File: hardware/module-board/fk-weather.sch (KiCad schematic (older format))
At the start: 99 parts, among them J1 MICRO-USB, J2 CONN_01X03, J3 CONN_01X06, J4 Conn_01x02, J5 Conn_01x01, J6 CONN-HDR-2x5, J7 Conn_01x01, J8 Conn_01x01, J9 Conn_01x01, M1 MOUNT_HOLE, M2 MOUNT_HOLE, M3 MOUNT_HOLE, M4 MOUNT_HOLE, Q1 2N7002LT1G, Q2 2N7002LT1G, Q3 2N7002LT1G, Q4 2N7002LT1G, SW1 SPNO, U1 ATSAMD21G18A-AU, U101 TSL2591, U102 MPL3115A2, U103 BNO055, U104 SHT31, U2 MCP1700T-XXX2E, U3 MAX4466, U4 S25FL1xxK0XM, Y1 FC-135, Y101 FC-135

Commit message: Adding PCB/sch for the wind/rain connectors.
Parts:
- removed C105, C107: 22pF, Capacitors_SMD:C_0603_HandSoldering, symbol CAPACITOR-CERAMIC
- removed C106, C108: 100nF, Capacitors_SMD:C_0603_HandSoldering, symbol CAPACITOR-CERAMIC
- removed J5, J8: Conn_01x01, Measurement_Points:Measurement_Point_Round-SMD-Pad_Small, symbol Conn_01x01
- removed R101, R102, R103: 10K, Resistors_SMD:R_0603_HandSoldering, symbol RESISTOR
- removed R26, R27: 4.7K, Resistors_SMD:R_0603_HandSoldering, symbol RESISTOR
- removed U103: BNO055, conservify:BNO055, symbol BNO055-RESCUE-fk-weather
- removed Y101: FC-135, RocketScreamKicadLibrary:ABS07, symbol CRYSTAL
- added D10, D11, D6, D7, D8, D9: DIODE, RocketScreamKicadLibrary:SOD-123, symbol DIODE
- added J10, J11: Conn_01x06, conservify:wurth_615006138421, symbol Conn_01x06
- added R30, R31, R32, R33, R34: 1K, Resistors_SMD:R_0603_HandSoldering, symbol RESISTOR
- R22, R23: value 0R -> 1K; footprint conservify:SJ_SHORTED -> Resistors_SMD:R_0603_HandSoldering; spn1 (none) -> 603-RC0603FR-07330RL
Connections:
- net labels added: FLASH_CS, RAIN, RAIN_2, RAIN_5, WIND_DIR, WIND_SPEED
- net labels removed: D10, D11, D5, D6, SCL2, SDA2
- wire segments 300 -> 297
- no-connect marks 15 -> 11
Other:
- moved on the sheet: C10, C101, C102, C103, C104, C11, C12, C13, C15, C16, C17, C18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

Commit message: Removing sensors from module board.
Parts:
- removed C101: 1uF, Capacitors_SMD:C_0603_HandSoldering, symbol CAPACITOR-CERAMIC
- removed C102, C103, C109: 100nF, Capacitors_SMD:C_0603_HandSoldering, symbol CAPACITOR-CERAMIC
- removed C104: 10uF, Capacitors_SMD:C_0603_HandSoldering, symbol CAPACITOR-CERAMIC
- removed R18, R19, R20, R21, R24, R25: 0R, conservify:SJ_SHORTED, symbol RESISTOR
- removed U101: TSL2591, Housings_DFN_QFN:DFN-6-1EP_2x2mm_Pitch0.65mm, symbol TSL2591
- removed U102: MPL3115A2, conservify:DFN-8-1EP_5x2.55mm_Pitch1.25mm_98ASA002260D, symbol MPL3115A2
- removed U104: SHT31, conservify:SHT3x, symbol SHT31
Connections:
- wire segments 297 -> 255
- no-connect marks 11 -> 7

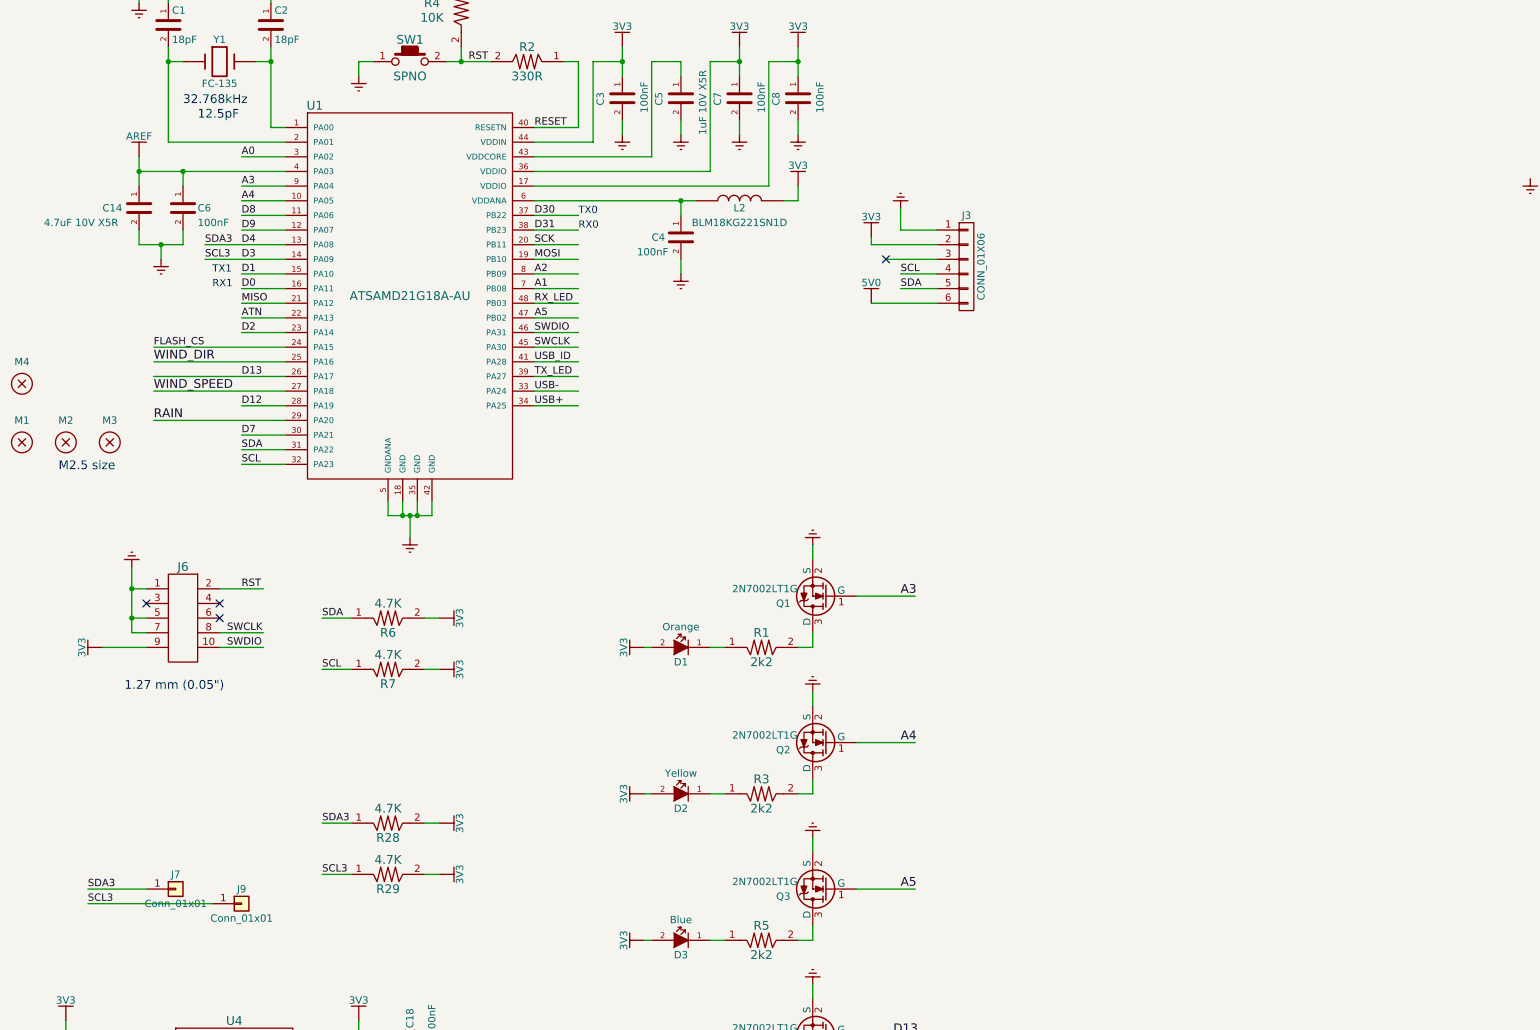
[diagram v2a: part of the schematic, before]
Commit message: Wire up the I2C buses to the header.
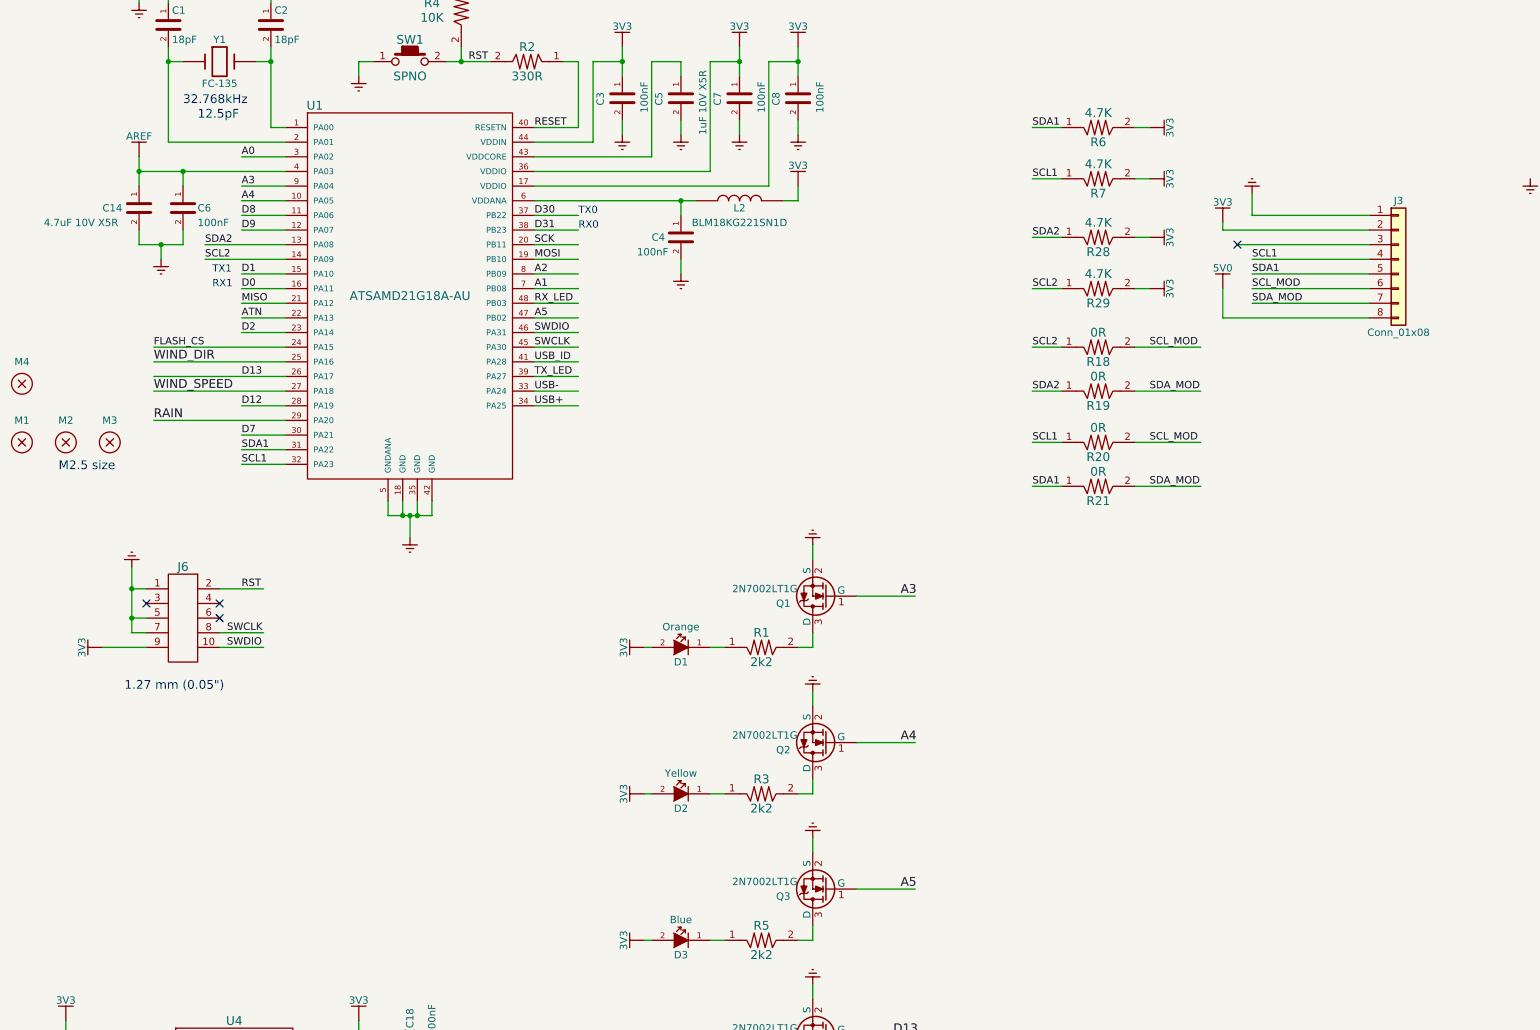
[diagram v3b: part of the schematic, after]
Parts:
- removed J3: CONN_01X06, Socket_Strips:Socket_Strip_Straight_1x06_Pitch2.54mm, symbol CONN_01X06
- removed J7, J9: Conn_01x01, Measurement_Points:Measurement_Point_Round-SMD-Pad_Small, symbol Conn_01x01
- added J3: Conn_01x08, Socket_Strips:Socket_Strip_Straight_1x08_Pitch2.54mm, symbol Conn_01x08
- added R18, R19, R20, R21: 0R, conservify:SJ_SHORTED, symbol RESISTOR
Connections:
- net labels added: SCL1, SCL2, SCL_MOD, SDA1, SDA2, SDA_MOD
- net labels removed: D3, D4, SCL, SCL3, SDA, SDA3
- wire segments 255 -> 264
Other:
- moved on the sheet: R28, R29, R6, R7

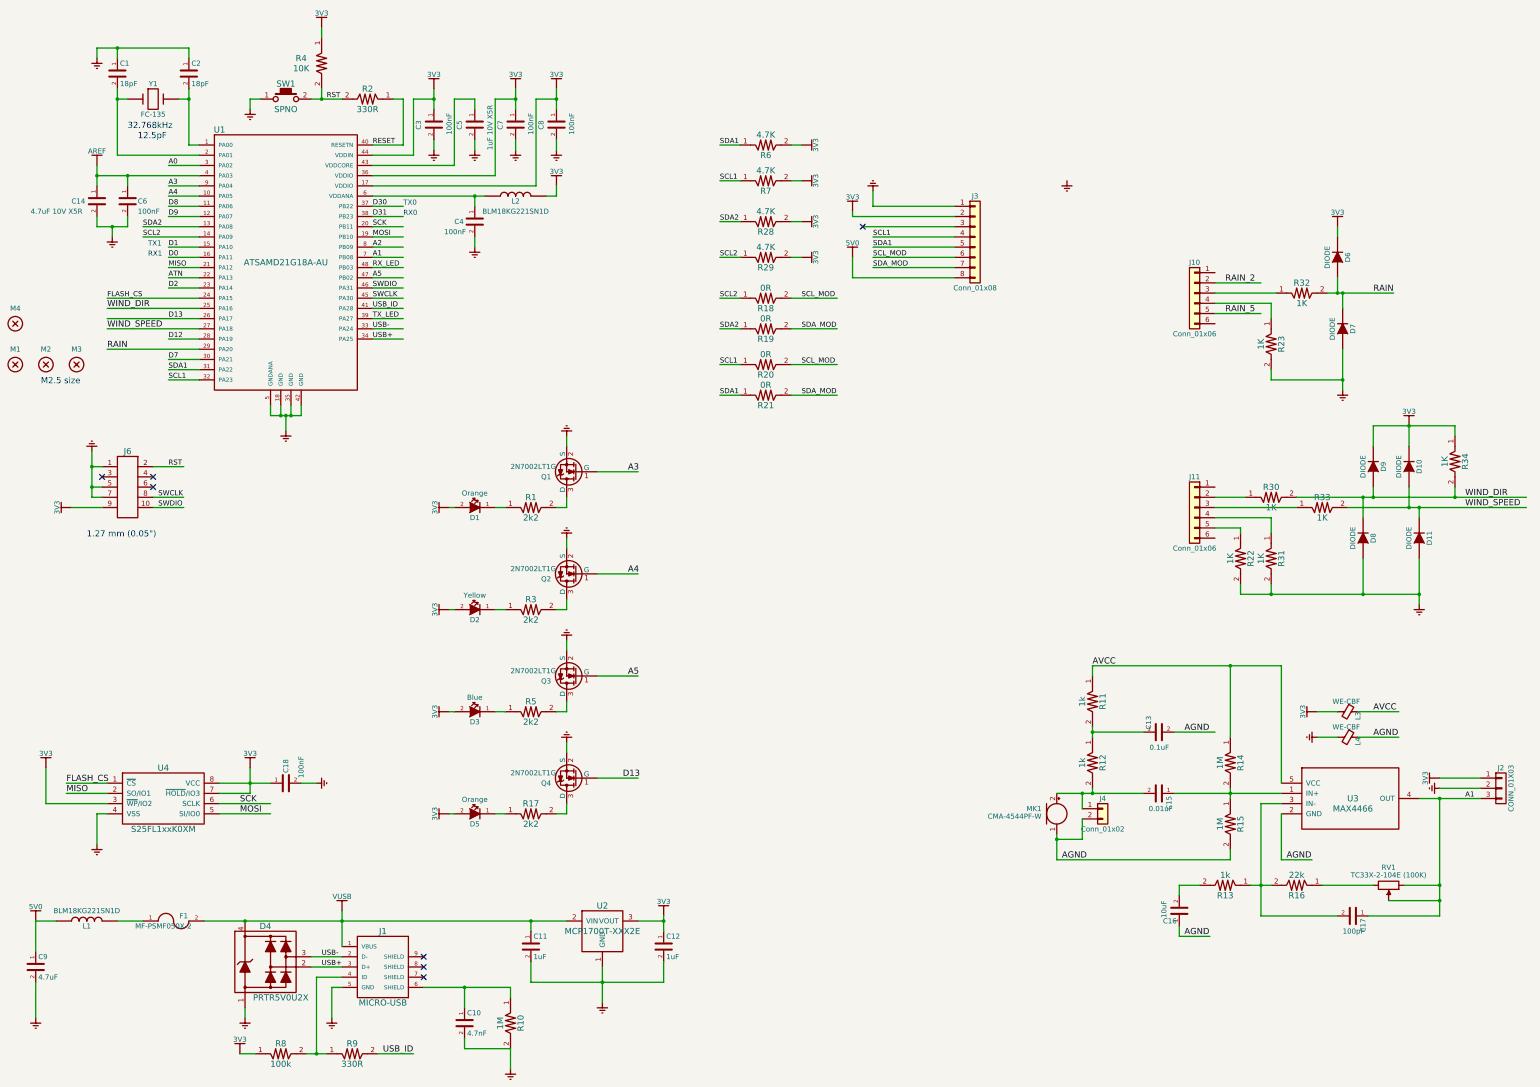
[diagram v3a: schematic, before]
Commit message: Fix RJ11 jacks. Clean up the board and I2C lines.
Got rid of the solder jumpers and just broke both out.
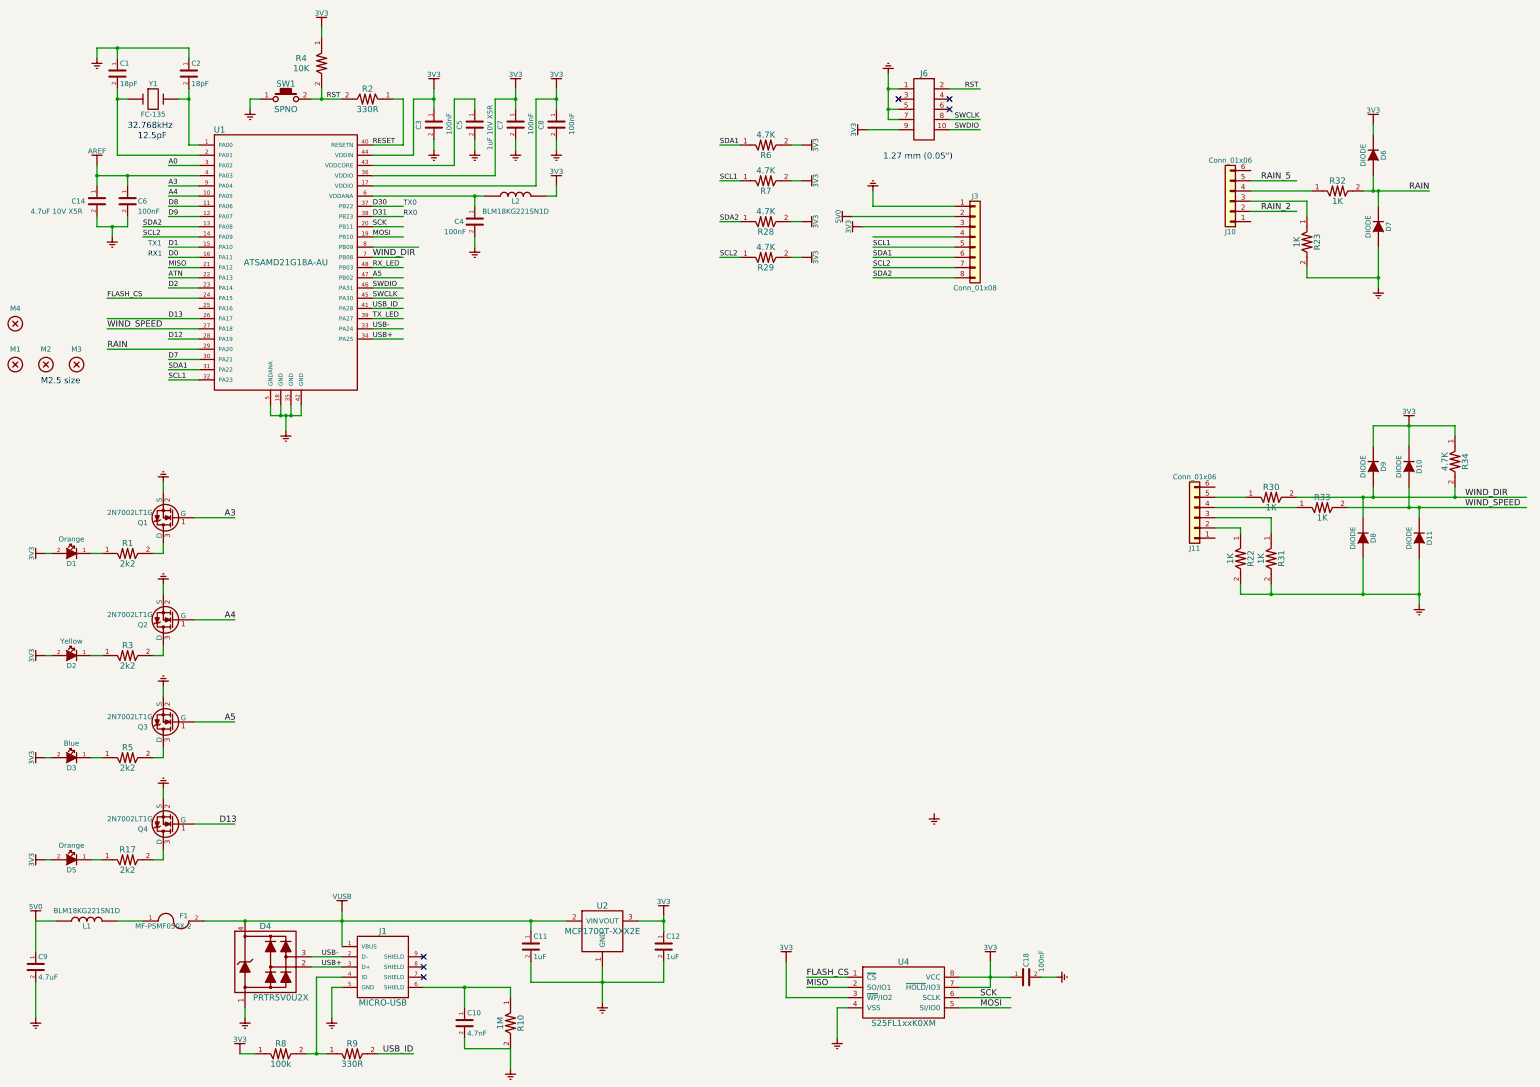
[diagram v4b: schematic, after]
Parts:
- removed C13: 0.1uF, Capacitors_SMD:C_0603_HandSoldering, symbol CAPACITOR-CERAMIC
- removed C15: 0.01uF, Capacitors_SMD:C_0603_HandSoldering, symbol CAPACITOR-CERAMIC
- removed C16: 10uF, Capacitors_SMD:C_0603_HandSoldering, symbol CAPACITOR-CERAMIC
- removed C17: 100pF, Capacitors_SMD:C_0603_HandSoldering, symbol CAPACITOR-CERAMIC
- removed J2: CONN_01X03, Socket_Strips:Socket_Strip_Straight_1x03_Pitch2.54mm, symbol CONN_01X03
- removed J4: Conn_01x02, Socket_Strips:Socket_Strip_Straight_2x01_Pitch2.54mm, symbol Conn_01x02
- removed L3, L4: WE-CBF, Resistors_SMD:R_0603_HandSoldering, symbol Ferrite_Bead_Small
- removed MK1: CMA-4544PF-W, Socket_Strips:Socket_Strip_Straight_1x02_Pitch2.54mm, symbol Microphone
- removed R11, R12, R13: 1k, Resistors_SMD:R_0603_HandSoldering, symbol RESISTOR
- removed R14, R15: 1M, Resistors_SMD:R_0603_HandSoldering, symbol RESISTOR
- removed R16: 22k, Resistors_SMD:R_0603_HandSoldering, symbol RESISTOR
- removed R18, R19, R20, R21: 0R, conservify:SJ_SHORTED, symbol RESISTOR
- removed RV1: TC33X-2-104E (100K), conservify:BOURNS-TC33X-2, symbol POT
- removed U3: MAX4466, conservify:SC70-5, symbol MAX4466
- R34: value 1K -> 4.7K
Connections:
- net labels removed: A1, A2, AGND, AVCC, SCL_MOD, SDA_MOD
- wire segments 264 -> 214
- no-connect marks 7 -> 6
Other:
- moved on the sheet: C18, D1, D2, D3, D5, D6, D7, J10, J6, Q1, Q2, Q3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

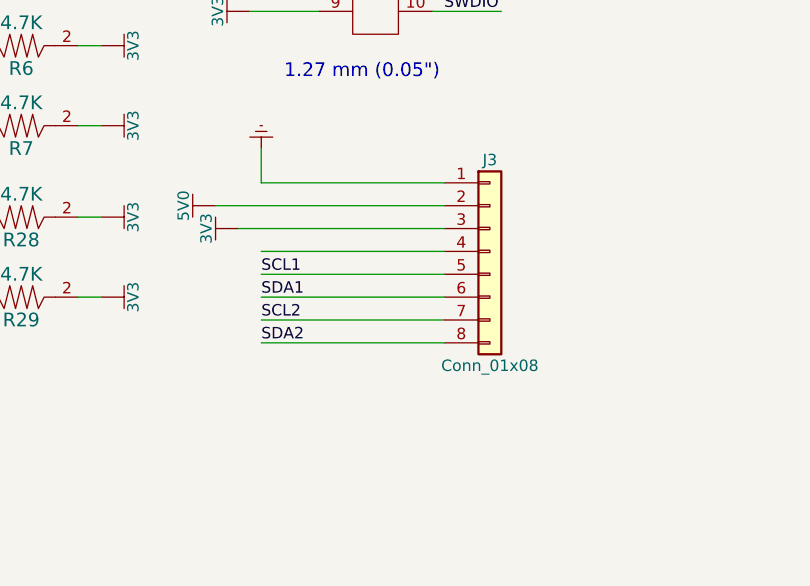
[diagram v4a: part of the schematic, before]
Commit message: Expose Serial2 (D31/D30)
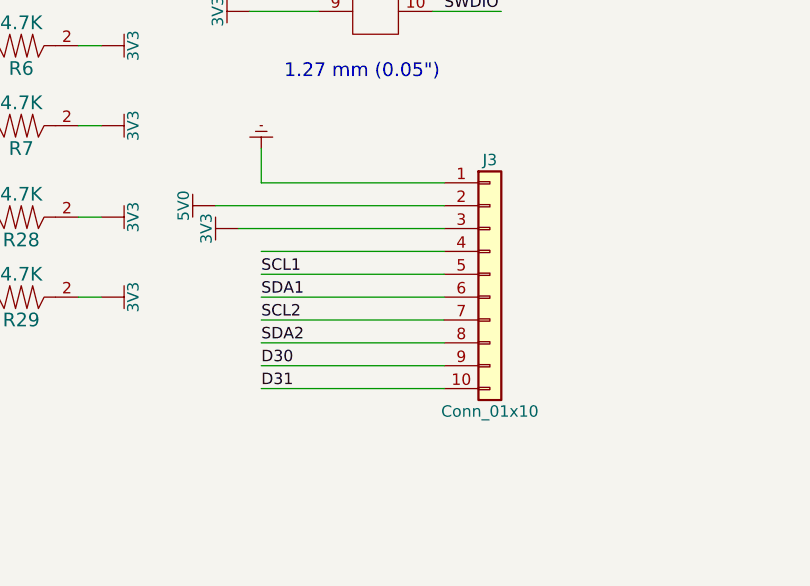
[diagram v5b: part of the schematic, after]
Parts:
- removed J3: Conn_01x08, Socket_Strips:Socket_Strip_Straight_1x08_Pitch2.54mm, symbol Conn_01x08
- added J3: Conn_01x10, Socket_Strips:Socket_Strip_Straight_1x10_Pitch2.54mm, symbol Conn_01x10
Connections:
- wire segments 214 -> 216
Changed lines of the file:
@@
 Text Label 1750 3950 0    60   ~ 0
 RAIN
-$Comp
-L Conn_01x08 J3
-U 1 1 5A46B966
-P 10250 2850
-F 0 "J3" H 10250 3250 50  0000 C CNN
-F 1 "Conn_01x08" H 10250 2350 50  0000 C CNN
-F 2 "Socket_Strips:Socket_Strip_Straight_1x08_Pitch2.54mm" H 10250 2850 50  0001 C CNN
-F 3 "" H 10250 2850 50  0001 C CNN
-	1    10250 2850
-	1    0    0    -1
-$EndComp
 Text Label 9250 3250 0    50   ~ 0
 SDA2
@@
 	1    0    0    -1
 $EndComp
+$Comp
+L Conn_01x10 J3
+U 1 1 5A454B4B
+P 10250 2950
+F 0 "J3" H 10250 3450 50  0000 C CNN
+F 1 "Conn_01x10" H 10250 2350 50  0000 C CNN
+F 2 "Socket_Strips:Socket_Strip_Straight_1x10_Pitch2.54mm" H 10250 2950 50  0001 C CNN
+F 3 "" H 10250 2950 50  0001 C CNN
+	1    10250 2950
+	1    0    0    -1
+$EndComp
+Text Label 9250 3450 0    50   ~ 0
+D31
+Text Label 9250 3350 0    50   ~ 0
+D30
+Wire Wire Line
+	10050 3350 9250 3350
+Wire Wire Line
+	9250 3450 10050 3450
 $EndSCHEMATC
